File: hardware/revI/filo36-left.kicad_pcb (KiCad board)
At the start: 2 copper layers, 113.7 x 89.4 mm, 46 parts, among them J1 BATTERY_PIGTAIL, J2 nice!view, K01 KEYSW, K02 KEYSW, K03 KEYSW, K04 KEYSW, K05 KEYSW, K11 KEYSW, K12 KEYSW, K13 KEYSW, K14 KEYSW, K15 KEYSW, K21 KEYSW, K22 KEYSW, K23 KEYSW, K24 KEYSW, K25 KEYSW, K30 KEYSW, K31 KEYSW, K32 KEYSW, SW1 SW_SPDT_PCM12, SW2 SW_SPST_TL3342, U1 nice!nano v2

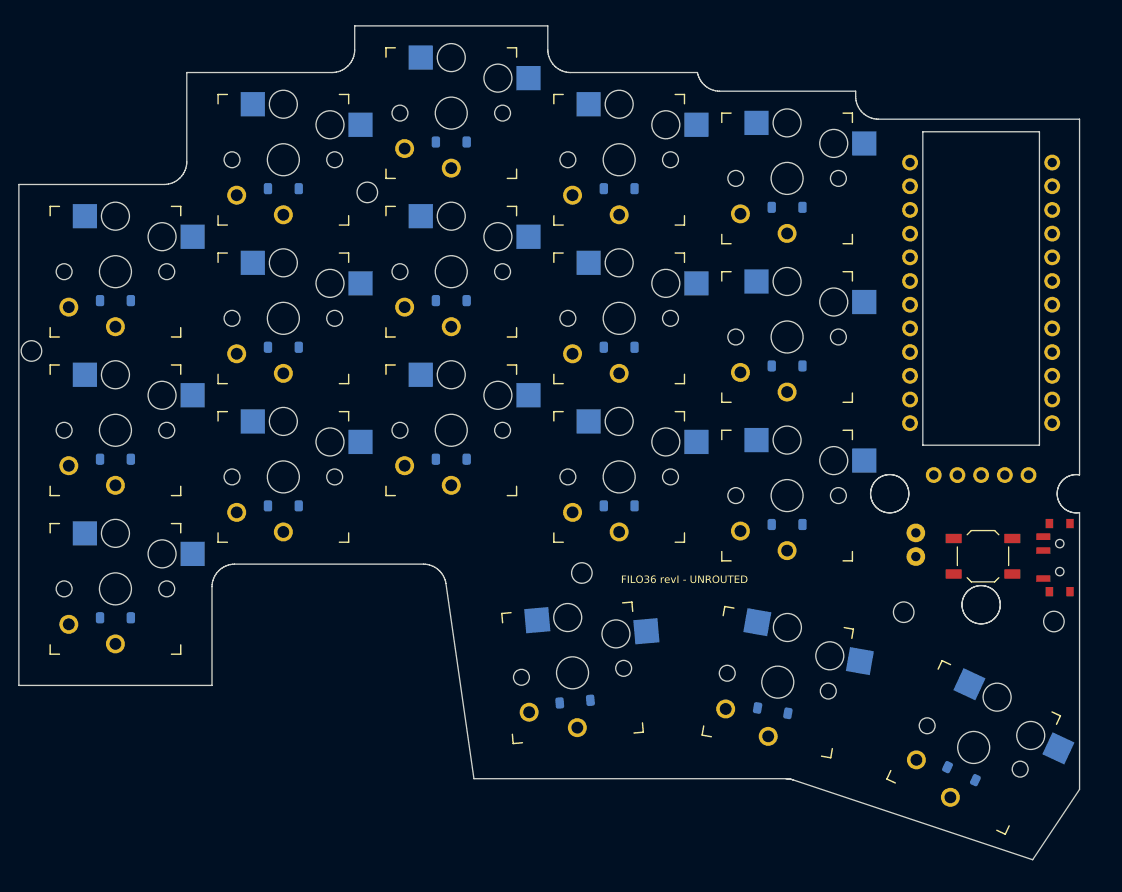
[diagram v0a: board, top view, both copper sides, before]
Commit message: Derive a uniform case rim from the switch openings
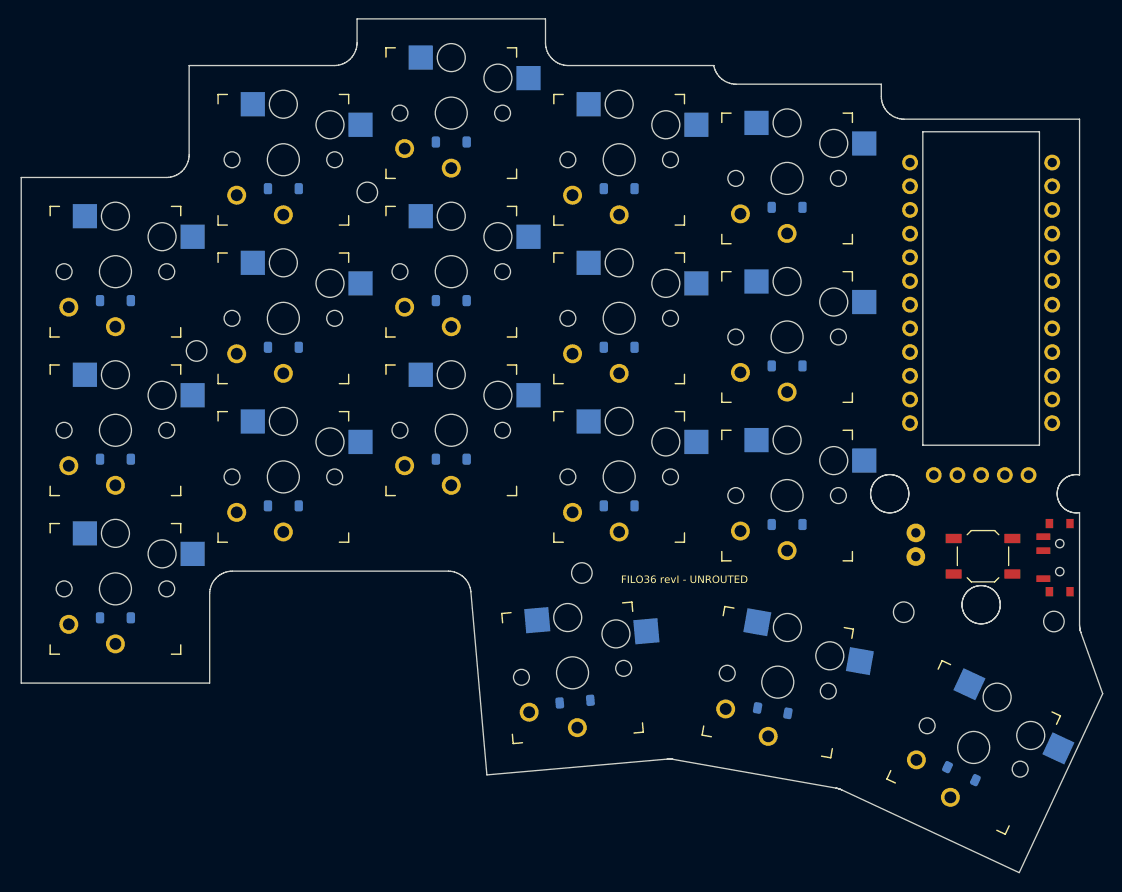
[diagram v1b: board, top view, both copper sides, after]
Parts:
- moved H1 17.7 mm to (38.7, 37.5)
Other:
- board size 113.7 x 89.4 mm -> 115.9 x 91.5 mm

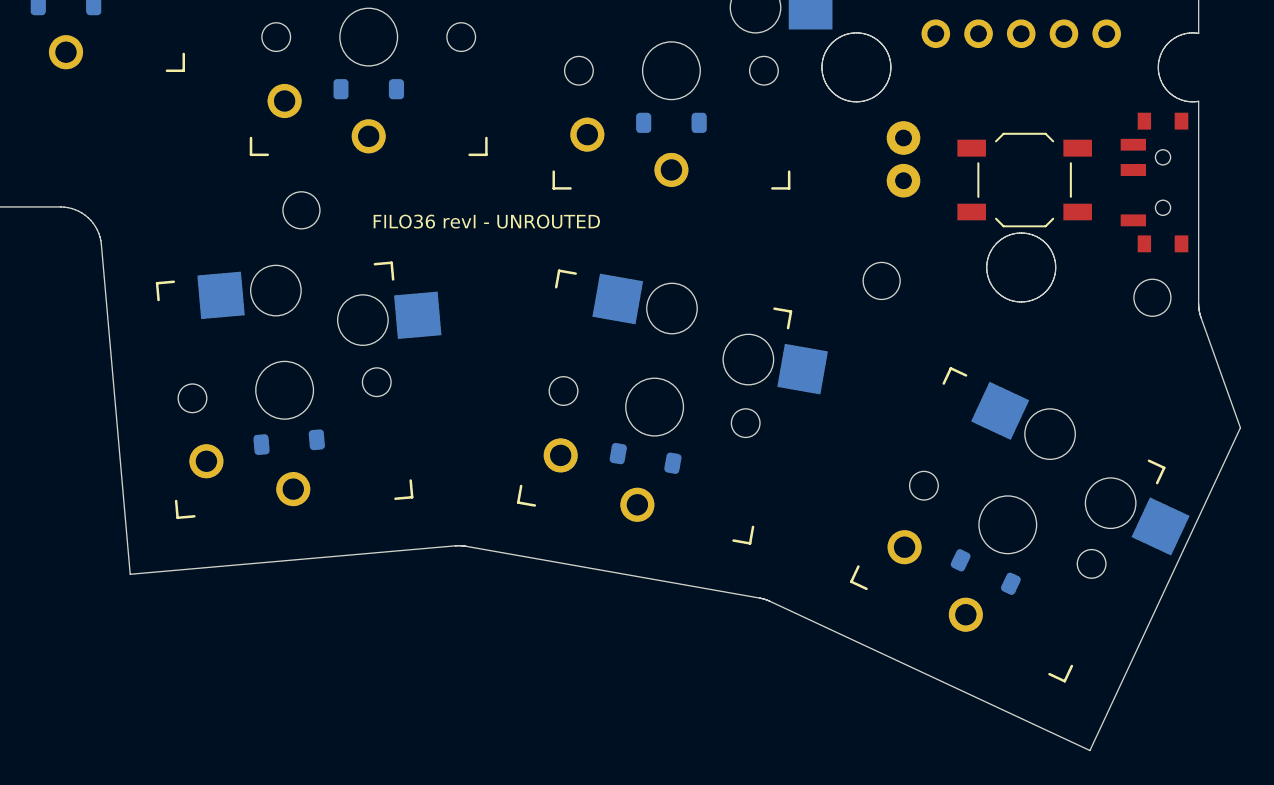
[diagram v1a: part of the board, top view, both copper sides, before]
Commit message: Curve thumb contour and add persistent per-part viewer controls
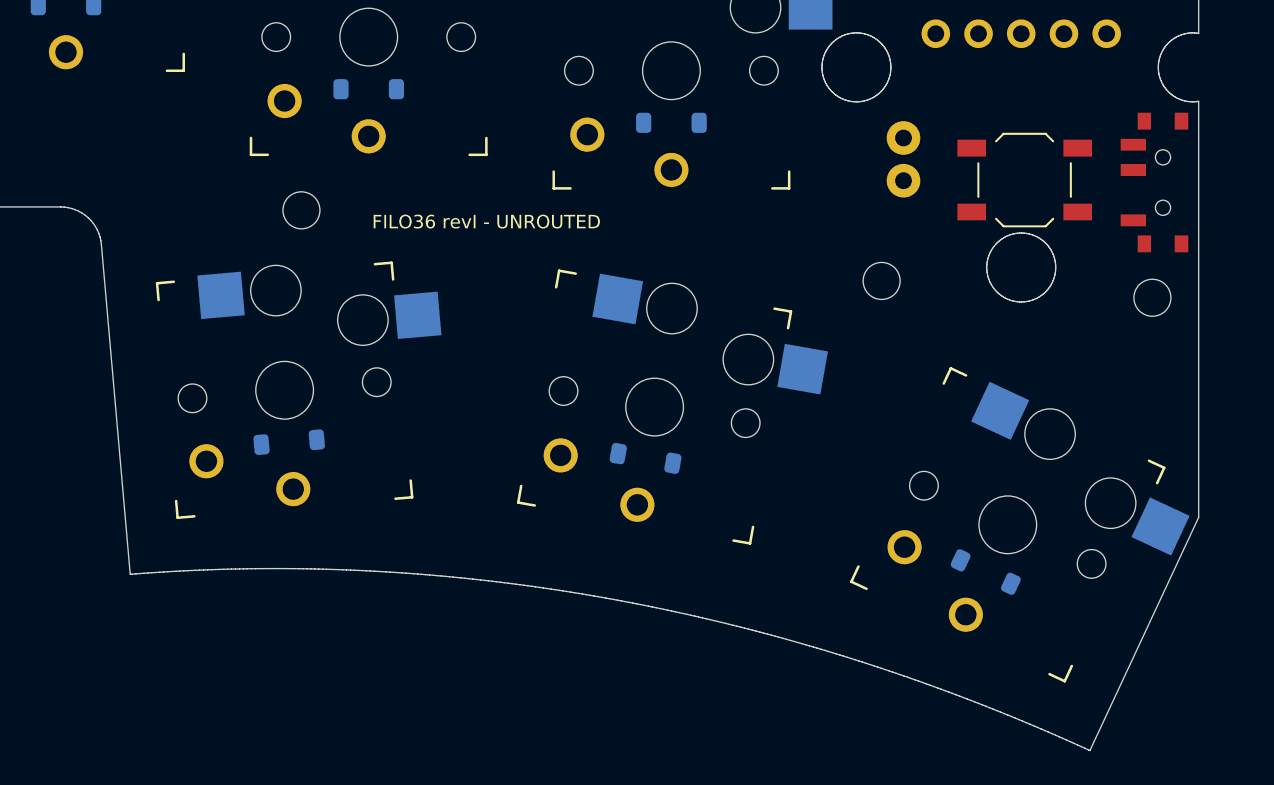
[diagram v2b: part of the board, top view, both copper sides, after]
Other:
- board size 115.9 x 91.5 mm -> 113.4 x 91.5 mm

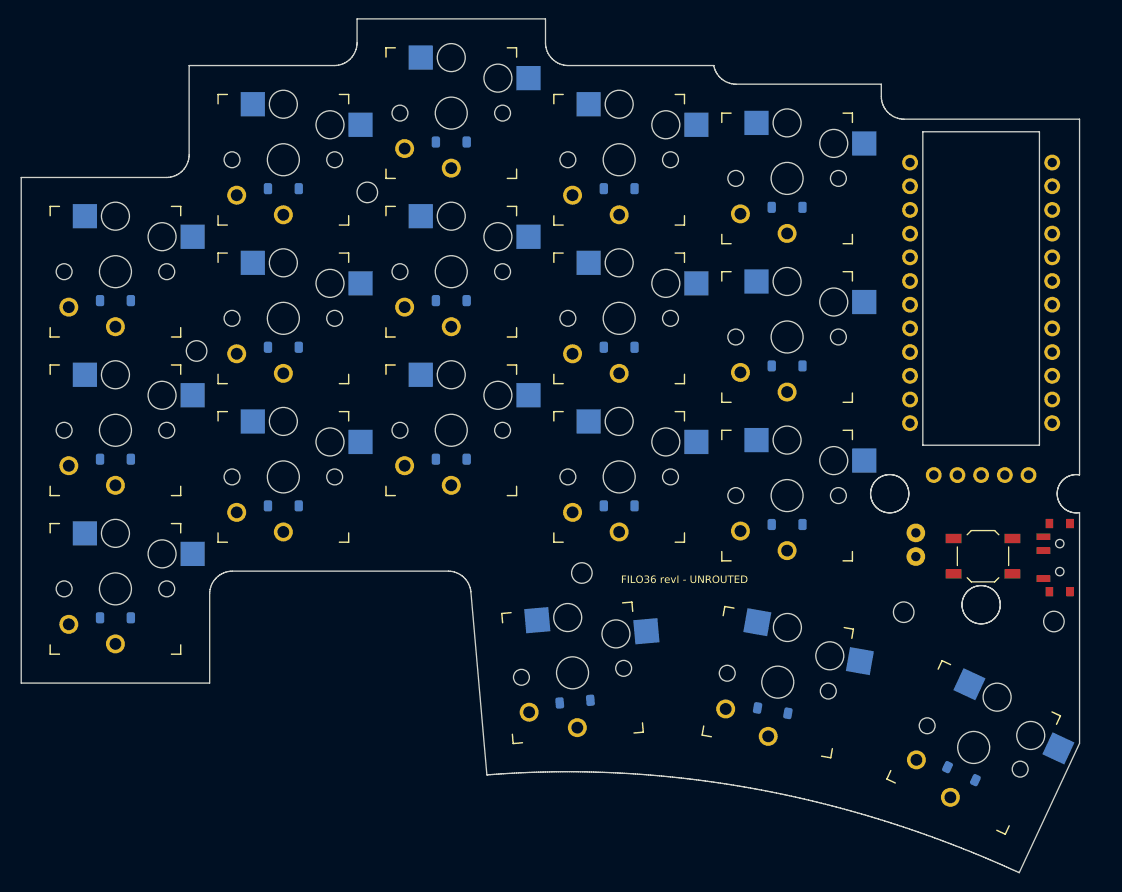
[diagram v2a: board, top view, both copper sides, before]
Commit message: Align case curves to keys and add interchangeable case designs
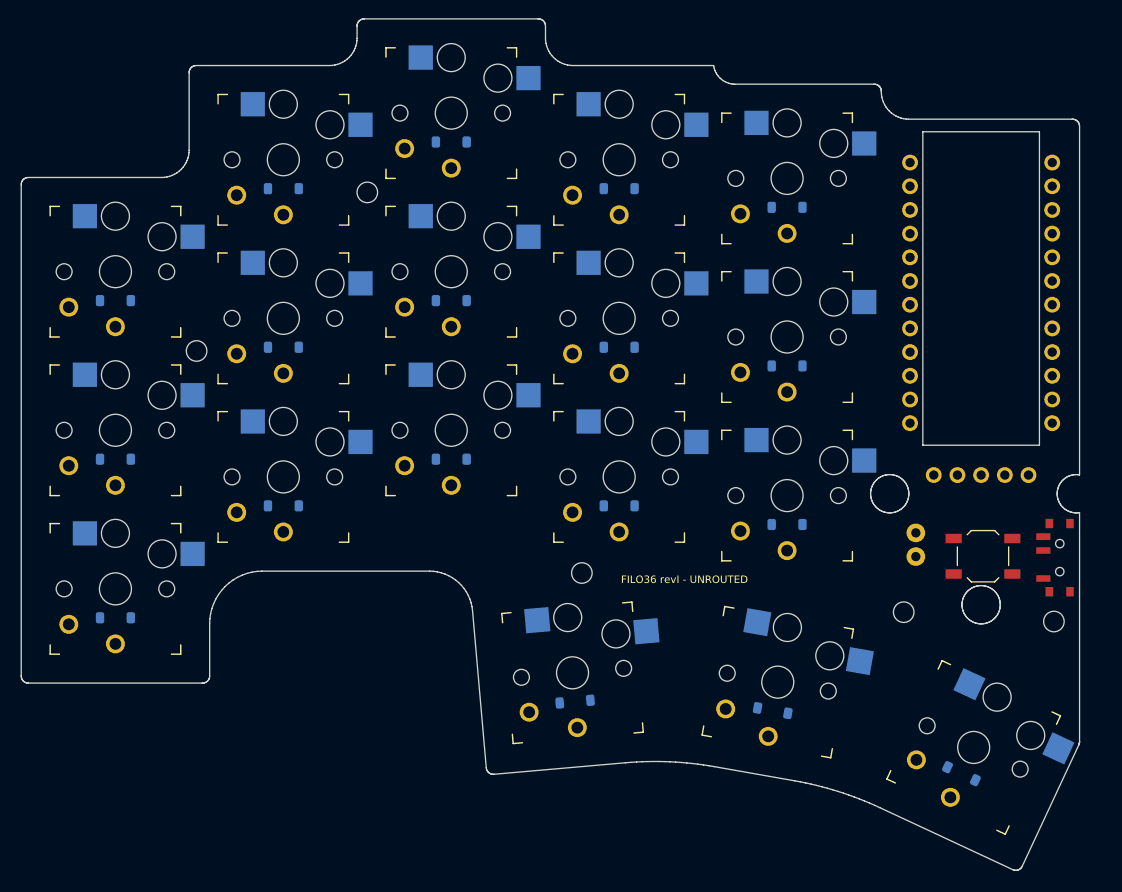
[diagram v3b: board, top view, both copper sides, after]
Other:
- board size 113.4 x 91.5 mm -> 113.4 x 91.3 mm
